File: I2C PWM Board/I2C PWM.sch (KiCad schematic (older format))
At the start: 34 parts, among them U1 PCA9685, U2 LD1117S33TR

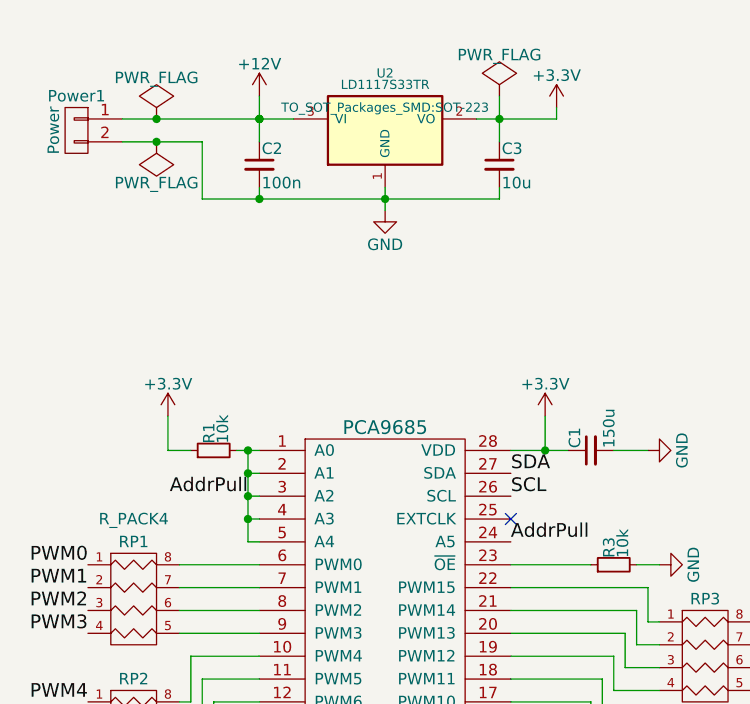
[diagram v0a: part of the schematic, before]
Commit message: Actually Add I2C-PWM Board
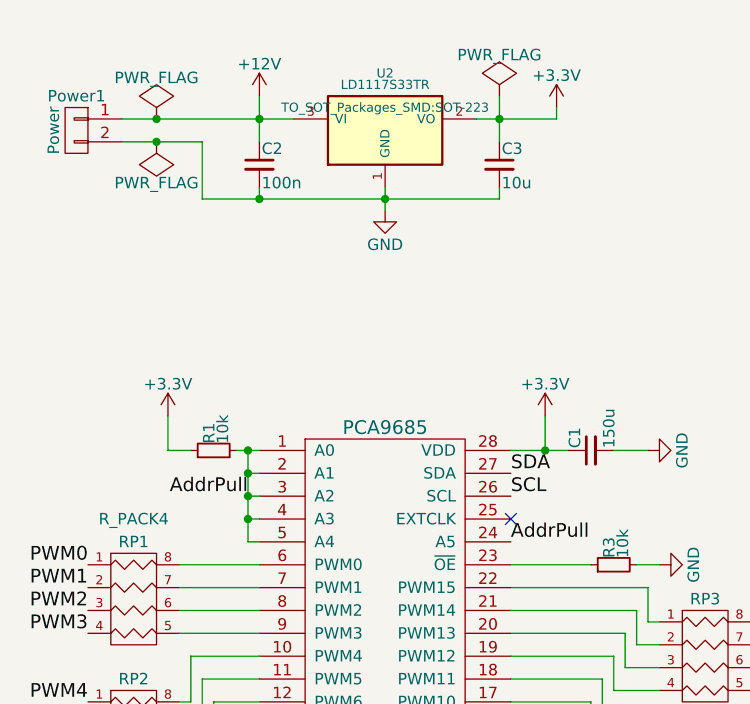
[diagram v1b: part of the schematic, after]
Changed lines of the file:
@@
 	1550 2650 1650 2650
 Wire Wire Line
-	1850 2650 1900 2650
+	1850 2650 1950 2650
 Wire Wire Line
-	1900 2650 1950 2650
-Wire Wire Line
-	1900 2650 1900 2750
-Wire Wire Line
-	1900 2750 1900 2850
-Wire Wire Line
-	1900 2850 1900 2950
-Wire Wire Line
-	1900 2950 1900 3050
+	1900 2650 1900 3050
 Wire Wire Line
 	1900 2750 1950 2750
@@
 	3200 2500 3200 2650
 Wire Wire Line
-	3050 2650 3200 2650
-Wire Wire Line
-	3200 2650 3300 2650
+	3050 2650 3300 2650
 Connection ~ 3200 2650
 Wire Wire Line
@@
 	3300 4300 3700 4300
 Wire Wire Line
-	1350 1200 1500 1200
-Wire Wire Line
-	1500 1200 1950 1200
-Wire Wire Line
-	1950 1200 1950 1200
-Wire Wire Line
-	1950 1200 2100 1200
+	1350 1200 2100 1200
 Connection ~ 1500 1200
 Wire Wire Line
-	1350 1300 1500 1300
-Wire Wire Line
-	1500 1300 1700 1300
+	1350 1300 1700 1300
 Connection ~ 1500 1300
 Wire Wire Line
@@
 	1950 5600 1800 5600
 Wire Wire Line
-	2500 1600 2500 1550
-Wire Wire Line
-	2500 1550 2500 1500
+	2500 1500 2500 1600
 Wire Wire Line
 	1700 1300 1700 1550
@@
 	1950 1500 1950 1550
 Wire Wire Line
-	1950 1300 1950 1200
+	1950 1100 1950 1300
 Connection ~ 1950 1200
 Wire Wire Line
-	3000 1100 3000 1200
-Wire Wire Line
-	3000 1200 3000 1300
+	3000 1100 3000 1300
 Wire Wire Line
 	3000 1550 3000 1500
@@
 	1    0    0    -1
 $EndComp
-Wire Wire Line
-	1950 1100 1950 1200
-Connection ~ 1950 1200
 $Comp
 L +3.3V #PWR029
@@
 3.3vPass
 Wire Wire Line
-	1700 1550 1950 1550
-Wire Wire Line
-	1950 1550 2500 1550
-Wire Wire Line
-	2500 1550 3000 1550
+	1700 1550 3000 1550
 Connection ~ 2500 1550
 Connection ~ 1950 1550
 Wire Wire Line
-	2900 1200 3000 1200
-Wire Wire Line
-	3000 1200 3250 1200
+	2900 1200 3250 1200
 Connection ~ 3000 1200
 $EndSCHEMATC
